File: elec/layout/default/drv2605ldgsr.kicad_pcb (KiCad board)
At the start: 2 copper layers, 225.7 x 100.8 mm, 3 parts

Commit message: layout
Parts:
- moved C2 4.24 mm to (159.6, 90.5), turned to 180 degrees
- moved C1 3.79 mm to (157.7, 90.5), turned to 0 degrees
- moved U1 0.94 mm to (158.8, 92.7), turned to -90 degrees
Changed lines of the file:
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@@
   (net 9 "n")
   (footprint "lib:C0402" (layer "F.Cu")
-    (at 155.566181 91.641436 -90)
+    (at 159.633564 90.451181 180)
     (descr "Capacitor SMD 0402 (1005 Metric), square (rectangular) end terminal, IPC_7351 nominal, (Body size source: IPC-SM-782 page 76, https://www.pcb-3d.com/wordpress/wp-content/uploads/ipc-sm-782a_amendment_1_and_2.pdf), generated with kicad-footprint-generator")
     (tags "capacitor")
     (attr smd)
-    (fp_text reference "C2" (at 0 -1.16 90) (layer "F.SilkS")
+    (fp_text reference "C2" (at 0 -1.16) (layer "F.SilkS")
         (effects (font (size 1 1) (thickness 0.15)))
     )
-    (fp_text value "Multilayer Ceramic Capacitors MLCC - SMD/SMT 1uF 6.3V 0402 RoHS" (at 0 1.16 90) (layer "F.Fab")
+    (fp_text value "Multilayer Ceramic Capacitors MLCC - SMD/SMT 1uF 6.3V 0402 RoHS" (at 0 1.16) (layer "F.Fab")
         (effects (font (size 1 1) (thickness 0.15)))
     )
-    (fp_text user "${REFERENCE}" (at 0 0 90) (layer "F.Fab")
+    (fp_text user "${REFERENCE}" (at 0 0) (layer "F.Fab")
         (effects (font (size 0.25 0.25) (thickness 0.04)))
     )
@@
     (fp_line (start 0.5 0.25) (end -0.5 0.25)
       (stroke (width 0.1) (type solid)) (layer "F.Fab"))
-    (pad "1" smd roundrect (at -0.48 0 270) (size 0.56 0.62) (layers "F.Cu" "F.Paste" "F.Mask") (roundrect_rratio 0.25)
+    (pad "1" smd roundrect (at -0.48 0 180) (size 0.56 0.62) (layers "F.Cu" "F.Paste" "F.Mask") (roundrect_rratio 0.25)
       (net 1 "vcc") (pintype "stereo"))
-    (pad "2" smd roundrect (at 0.48 0 270) (size 0.56 0.62) (layers "F.Cu" "F.Paste" "F.Mask") (roundrect_rratio 0.25)
+    (pad "2" smd roundrect (at 0.48 0 180) (size 0.56 0.62) (layers "F.Cu" "F.Paste" "F.Mask") (roundrect_rratio 0.25)
       (net 8 "gnd") (pintype "stereo"))
     (model "${KICAD6_3DMODEL_DIR}/Capacitor_SMD.3dshapes/C_0402_1005Metric.wrl"
@@
   )
   (footprint "lib:VSSOP-10_L3.0-W3.0-P0.50-LS4.9-BL" (layer "F.Cu")
-    (at 157.825 92.525)
+    (at 158.75 92.71 -90)
     (attr smd)
-    (fp_text reference "U1" (at 0 -6.35) (layer "F.SilkS")
+    (fp_text reference "U1" (at 0 -6.35 90) (layer "F.SilkS")
         (effects (font (size 1 1) (thickness 0.15)))
     )
-    (fp_text value "" (at 0 6.35) (layer "F.Fab")
+    (fp_text value "" (at 0 6.35 90) (layer "F.Fab")
         (effects (font (size 1 1) (thickness 0.15)))
     )
-    (fp_text user "${REFERENCE}" (at 0 0) (layer "F.Fab")
+    (fp_text user "${REFERENCE}" (at 0 0 90) (layer "F.Fab")
         (effects (font (size 1 1) (thickness 0.15)))
     )
@@
     (fp_circle (center -1.5 2.45) (end -1.47 2.45)
       (stroke (width 0.06) (type solid)) (fill none) (layer "F.Fab"))
-    (pad "1" smd rect (at -1 2.35) (size 0.3 1.3) (layers "F.Cu" "F.Paste" "F.Mask")
+    (pad "1" smd rect (at -1 2.35 270) (size 0.3 1.3) (layers "F.Cu" "F.Paste" "F.Mask")
       (net 1 "vcc") (pintype "stereo"))
-    (pad "2" smd rect (at -0.5 2.35) (size 0.3 1.3) (layers "F.Cu" "F.Paste" "F.Mask")
+    (pad "2" smd rect (at -0.5 2.35 270) (size 0.3 1.3) (layers "F.Cu" "F.Paste" "F.Mask")
       (net 2 "scl") (pintype "stereo"))
-    (pad "3" smd rect (at 0 2.35) (size 0.3 1.3) (layers "F.Cu" "F.Paste" "F.Mask")
+    (pad "3" smd rect (at 0 2.35 270) (size 0.3 1.3) (layers "F.Cu" "F.Paste" "F.Mask")
       (net 3 "sda") (pintype "stereo"))
-    (pad "4" smd rect (at 0.5 2.35) (size 0.3 1.3) (layers "F.Cu" "F.Paste" "F.Mask")
+    (pad "4" smd rect (at 0.5 2.35 270) (size 0.3 1.3) (layers "F.Cu" "F.Paste" "F.Mask")
       (net 4 "in_trig") (pintype "stereo"))
-    (pad "5" smd rect (at 1 2.35) (size 0.3 1.3) (layers "F.Cu" "F.Paste" "F.Mask")
+    (pad "5" smd rect (at 1 2.35 270) (size 0.3 1.3) (layers "F.Cu" "F.Paste" "F.Mask")
       (net 5 "en") (pintype "stereo"))
-    (pad "6" smd rect (at 1 -2.35) (size 0.3 1.3) (layers "F.Cu" "F.Paste" "F.Mask")
+    (pad "6" smd rect (at 1 -2.35 270) (size 0.3 1.3) (layers "F.Cu" "F.Paste" "F.Mask")
       (net 6 "vdd_nc") (pintype "stereo"))
-    (pad "7" smd rect (at 0.5 -2.35) (size 0.3 1.3) (layers "F.Cu" "F.Paste" "F.Mask")
+    (pad "7" smd rect (at 0.5 -2.35 270) (size 0.3 1.3) (layers "F.Cu" "F.Paste" "F.Mask")
       (net 7 "p") (pintype "stereo"))
-    (pad "8" smd rect (at 0 -2.35) (size 0.3 1.3) (layers "F.Cu" "F.Paste" "F.Mask")
+    (pad "8" smd rect (at 0 -2.35 270) (size 0.3 1.3) (layers "F.Cu" "F.Paste" "F.Mask")
       (net 8 "gnd") (pintype "stereo"))
-    (pad "9" smd rect (at -0.5 -2.35) (size 0.3 1.3) (layers "F.Cu" "F.Paste" "F.Mask")
+    (pad "9" smd rect (at -0.5 -2.35 270) (size 0.3 1.3) (layers "F.Cu" "F.Paste" "F.Mask")
       (net 9 "n") (pintype "stereo"))
-    (pad "10" smd rect (at -1 -2.35) (size 0.3 1.3) (layers "F.Cu" "F.Paste" "F.Mask")
+    (pad "10" smd rect (at -1 -2.35 270) (size 0.3 1.3) (layers "F.Cu" "F.Paste" "F.Mask")
       (net 1 "vcc") (pintype "stereo"))
     (model "/Users/narayanpowderly/Documents/atopile-workspace/swoop/.ato/modules/drv2605ldgsr/elec/footprints/footprints.3dshapes/VSSOP-10_L3.0-W3.0-H1.1-LS4.9-P0.50.wrl"
@@
   )
   (footprint "lib:C0402" (layer "F.Cu")
-    (at 155.566181 93.595775 90)
+    (at 157.679225 90.451181)
     (descr "Capacitor SMD 0402 (1005 Metric), square (rectangular) end terminal, IPC_7351 nominal, (Body size source: IPC-SM-782 page 76, https://www.pcb-3d.com/wordpress/wp-content/uploads/ipc-sm-782a_amendment_1_and_2.pdf), generated with kicad-footprint-generator")
     (tags "capacitor")
     (attr smd)
-    (fp_text reference "C1" (at 0 -1.16 90) (layer "F.SilkS")
+    (fp_text reference "C1" (at 0 -1.16) (layer "F.SilkS")
         (effects (font (size 1 1) (thickness 0.15)))
     )
-    (fp_text value "Multilayer Ceramic Capacitors MLCC - SMD/SMT 1uF 6.3V 0402 RoHS" (at 0 1.16 90) (layer "F.Fab")
+    (fp_text value "Multilayer Ceramic Capacitors MLCC - SMD/SMT 1uF 6.3V 0402 RoHS" (at 0 1.16) (layer "F.Fab")
         (effects (font (size 1 1) (thickness 0.15)))
     )
-    (fp_text user "${REFERENCE}" (at 0 0 90) (layer "F.Fab")
+    (fp_text user "${REFERENCE}" (at 0 0) (layer "F.Fab")
         (effects (font (size 0.25 0.25) (thickness 0.04)))
     )
@@
     (fp_line (start 0.5 0.25) (end -0.5 0.25)
       (stroke (width 0.1) (type solid)) (layer "F.Fab"))
-    (pad "1" smd roundrect (at -0.48 0 90) (size 0.56 0.62) (layers "F.Cu" "F.Paste" "F.Mask") (roundrect_rratio 0.25)
+    (pad "1" smd roundrect (at -0.48 0) (size 0.56 0.62) (layers "F.Cu" "F.Paste" "F.Mask") (roundrect_rratio 0.25)
       (net 1 "vcc") (pintype "stereo"))
-    (pad "2" smd roundrect (at 0.48 0 90) (size 0.56 0.62) (layers "F.Cu" "F.Paste" "F.Mask") (roundrect_rratio 0.25)
+    (pad "2" smd roundrect (at 0.48 0) (size 0.56 0.62) (layers "F.Cu" "F.Paste" "F.Mask") (roundrect_rratio 0.25)
       (net 8 "gnd") (pintype "stereo"))
     (model "${KICAD6_3DMODEL_DIR}/Capacitor_SMD.3dshapes/C_0402_1005Metric.wrl"
@@
     (effects (font (size 2 2) (thickness 0.1)) (justify left bottom))
   )
-  (segment (start 156.365406 94.875) (end 155.566181 94.075775) (width 0.25) (layer "F.Cu") (net 1))
-  (segment (start 154.931181 93.448384) (end 155.558572 94.075775) (width 0.25) (layer "F.Cu") (net 1))
-  (segment (start 156.825 94.875) (end 156.365406 94.875) (width 0.25) (layer "F.Cu") (net 1))
-  (segment (start 156.825 90.175) (end 156.552617 90.175) (width 0.25) (layer "F.Cu") (net 1))
-  (segment (start 155.558572 91.161436) (end 154.931181 91.788827) (width 0.25) (layer "F.Cu") (net 1))
-  (segment (start 155.558572 94.075775) (end 155.566181 94.075775) (width 0.25) (layer "F.Cu") (net 1))
-  (segment (start 154.931181 91.788827) (end 154.931181 93.448384) (width 0.25) (layer "F.Cu") (net 1))
-  (segment (start 155.566181 91.161436) (end 155.558572 91.161436) (width 0.25) (layer "F.Cu") (net 1))
-  (segment (start 156.552617 90.175) (end 155.566181 91.161436) (width 0.25) (layer "F.Cu") (net 1))
-  (segment (start 157.825 90.175) (end 157.825 91.125) (width 0.25) (layer "F.Cu") (net 8))
-  (segment (start 155.566181 93.115775) (end 155.566181 92.121436) (width 0.25) (layer "F.Cu") (net 8))
-  (segment (start 157.825 91.125) (end 156.828564 92.121436) (width 0.25) (layer "F.Cu") (net 8))
-  (segment (start 156.828564 92.121436) (end 155.566181 92.121436) (width 0.25) (layer "F.Cu") (net 8))
+  (segment (start 156.4 91.250406) (end 157.199225 90.451181) (width 0.25) (layer "F.Cu") (net 1))
+  (segment (start 157.826616 89.816181) (end 157.199225 90.443572) (width 0.25) (layer "F.Cu") (net 1))
+  (segment (start 156.4 91.71) (end 156.4 91.250406) (width 0.25) (layer "F.Cu") (net 1))
+  (segment (start 161.1 91.71) (end 161.1 91.437617) (width 0.25) (layer "F.Cu") (net 1))
+  (segment (start 160.113564 90.443572) (end 159.486173 89.816181) (width 0.25) (layer "F.Cu") (net 1))
+  (segment (start 157.199225 90.443572) (end 157.199225 90.451181) (width 0.25) (layer "F.Cu") (net 1))
+  (segment (start 159.486173 89.816181) (end 157.826616 89.816181) (width 0.25) (layer "F.Cu") (net 1))
+  (segment (start 160.113564 90.451181) (end 160.113564 90.443572) (width 0.25) (layer "F.Cu") (net 1))
+  (segment (start 161.1 91.437617) (end 160.113564 90.451181) (width 0.25) (layer "F.Cu") (net 1))
+  (segment (start 161.1 92.71) (end 160.15 92.71) (width 0.25) (layer "F.Cu") (net 8))
+  (segment (start 158.159225 90.451181) (end 159.153564 90.451181) (width 0.25) (layer "F.Cu") (net 8))
+  (segment (start 160.15 92.71) (end 159.153564 91.713564) (width 0.25) (layer "F.Cu") (net 8))
+  (segment (start 159.153564 91.713564) (end 159.153564 90.451181) (width 0.25) (layer "F.Cu") (net 8))
   (group "" (id 6c1ef9f7-0f34-47bb-ac1a-76df23fb396e)
     (members

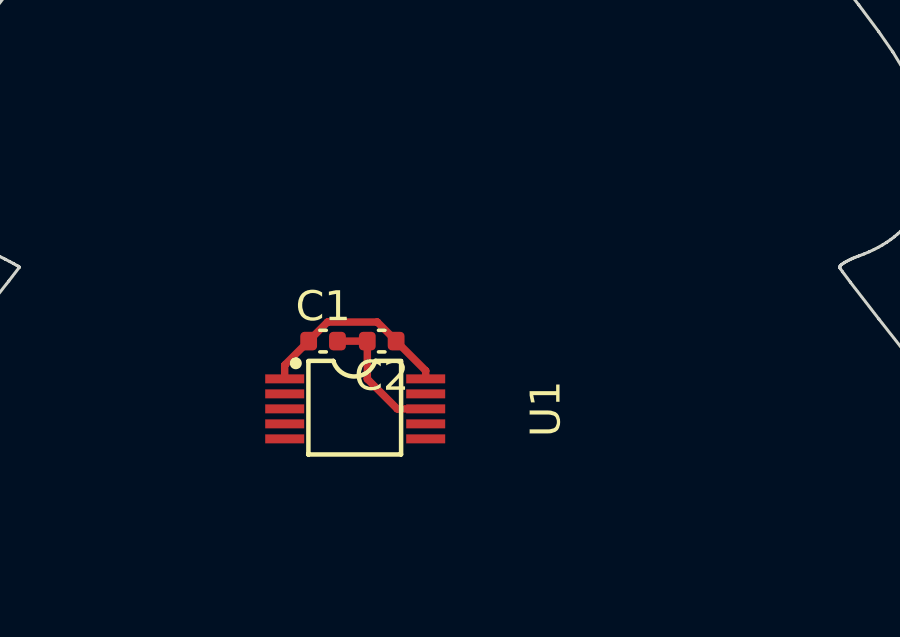
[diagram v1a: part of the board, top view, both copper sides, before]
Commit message: Fix index lock issue
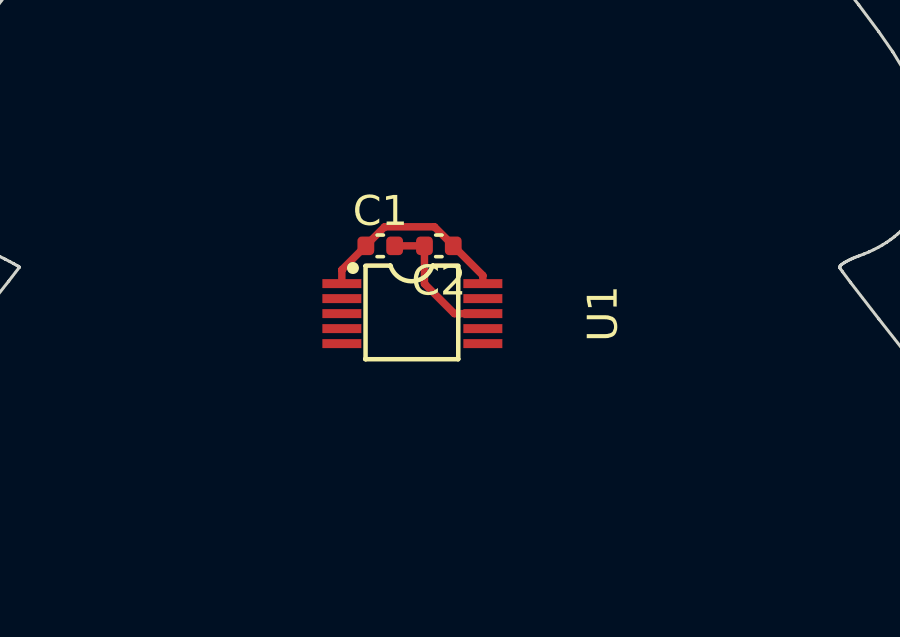
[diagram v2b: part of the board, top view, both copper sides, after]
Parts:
- moved C1 3.70 mm to (159.6, 87.3)
- moved C2 3.70 mm to (161.5, 87.3)
- moved U1 3.70 mm to (160.7, 89.5)
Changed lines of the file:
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@@
   (net 9 "n")
   (footprint "lib:C0402" (layer "F.Cu")
-    (at 159.633564 90.451181 180)
+    (at 161.538564 87.276181 180)
     (descr "Capacitor SMD 0402 (1005 Metric), square (rectangular) end terminal, IPC_7351 nominal, (Body size source: IPC-SM-782 page 76, https://www.pcb-3d.com/wordpress/wp-content/uploads/ipc-sm-782a_amendment_1_and_2.pdf), generated with kicad-footprint-generator")
     (tags "capacitor")
@@
   )
   (footprint "lib:VSSOP-10_L3.0-W3.0-P0.50-LS4.9-BL" (layer "F.Cu")
-    (at 158.75 92.71 -90)
+    (at 160.655 89.535 -90)
     (attr smd)
     (fp_text reference "U1" (at 0 -6.35 90) (layer "F.SilkS")
@@
   )
   (footprint "lib:C0402" (layer "F.Cu")
-    (at 157.679225 90.451181)
+    (at 159.584225 87.276181)
     (descr "Capacitor SMD 0402 (1005 Metric), square (rectangular) end terminal, IPC_7351 nominal, (Body size source: IPC-SM-782 page 76, https://www.pcb-3d.com/wordpress/wp-content/uploads/ipc-sm-782a_amendment_1_and_2.pdf), generated with kicad-footprint-generator")
     (tags "capacitor")
@@
     (effects (font (size 2 2) (thickness 0.1)) (justify left bottom))
   )
-  (segment (start 156.4 91.250406) (end 157.199225 90.451181) (width 0.25) (layer "F.Cu") (net 1))
-  (segment (start 157.826616 89.816181) (end 157.199225 90.443572) (width 0.25) (layer "F.Cu") (net 1))
-  (segment (start 156.4 91.71) (end 156.4 91.250406) (width 0.25) (layer "F.Cu") (net 1))
-  (segment (start 161.1 91.71) (end 161.1 91.437617) (width 0.25) (layer "F.Cu") (net 1))
-  (segment (start 160.113564 90.443572) (end 159.486173 89.816181) (width 0.25) (layer "F.Cu") (net 1))
-  (segment (start 157.199225 90.443572) (end 157.199225 90.451181) (width 0.25) (layer "F.Cu") (net 1))
-  (segment (start 159.486173 89.816181) (end 157.826616 89.816181) (width 0.25) (layer "F.Cu") (net 1))
-  (segment (start 160.113564 90.451181) (end 160.113564 90.443572) (width 0.25) (layer "F.Cu") (net 1))
-  (segment (start 161.1 91.437617) (end 160.113564 90.451181) (width 0.25) (layer "F.Cu") (net 1))
-  (segment (start 161.1 92.71) (end 160.15 92.71) (width 0.25) (layer "F.Cu") (net 8))
-  (segment (start 158.159225 90.451181) (end 159.153564 90.451181) (width 0.25) (layer "F.Cu") (net 8))
-  (segment (start 160.15 92.71) (end 159.153564 91.713564) (width 0.25) (layer "F.Cu") (net 8))
-  (segment (start 159.153564 91.713564) (end 159.153564 90.451181) (width 0.25) (layer "F.Cu") (net 8))
+  (segment (start 158.305 88.075406) (end 159.104225 87.276181) (width 0.25) (layer "F.Cu") (net 1))
+  (segment (start 159.731616 86.641181) (end 159.104225 87.268572) (width 0.25) (layer "F.Cu") (net 1))
+  (segment (start 158.305 88.535) (end 158.305 88.075406) (width 0.25) (layer "F.Cu") (net 1))
+  (segment (start 163.005 88.535) (end 163.005 88.262617) (width 0.25) (layer "F.Cu") (net 1))
+  (segment (start 162.018564 87.268572) (end 161.391173 86.641181) (width 0.25) (layer "F.Cu") (net 1))
+  (segment (start 159.104225 87.268572) (end 159.104225 87.276181) (width 0.25) (layer "F.Cu") (net 1))
+  (segment (start 161.391173 86.641181) (end 159.731616 86.641181) (width 0.25) (layer "F.Cu") (net 1))
+  (segment (start 162.018564 87.276181) (end 162.018564 87.268572) (width 0.25) (layer "F.Cu") (net 1))
+  (segment (start 163.005 88.262617) (end 162.018564 87.276181) (width 0.25) (layer "F.Cu") (net 1))
+  (segment (start 163.005 89.535) (end 162.055 89.535) (width 0.25) (layer "F.Cu") (net 8))
+  (segment (start 160.064225 87.276181) (end 161.058564 87.276181) (width 0.25) (layer "F.Cu") (net 8))
+  (segment (start 162.055 89.535) (end 161.058564 88.538564) (width 0.25) (layer "F.Cu") (net 8))
+  (segment (start 161.058564 88.538564) (end 161.058564 87.276181) (width 0.25) (layer "F.Cu") (net 8))
   (group "" (id 6c1ef9f7-0f34-47bb-ac1a-76df23fb396e)
     (members
